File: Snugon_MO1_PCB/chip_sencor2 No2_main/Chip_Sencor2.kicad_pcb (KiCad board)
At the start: 2 copper layers, 50.7 x 80 mm, 55 parts, among them J1 Conn_01x8_Pin + 2, J3 USB_C_Receptacle_USB2.0, J6 Conn_01x8_Pin + 2, SW0 SW_PUSH, SW1 SW_PUSH, U1 RP2040, U2 TPS73601DBV, U3 TXS0102DCU, U4 TXS0102DCU, U5 PMW3360DM-T2QU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

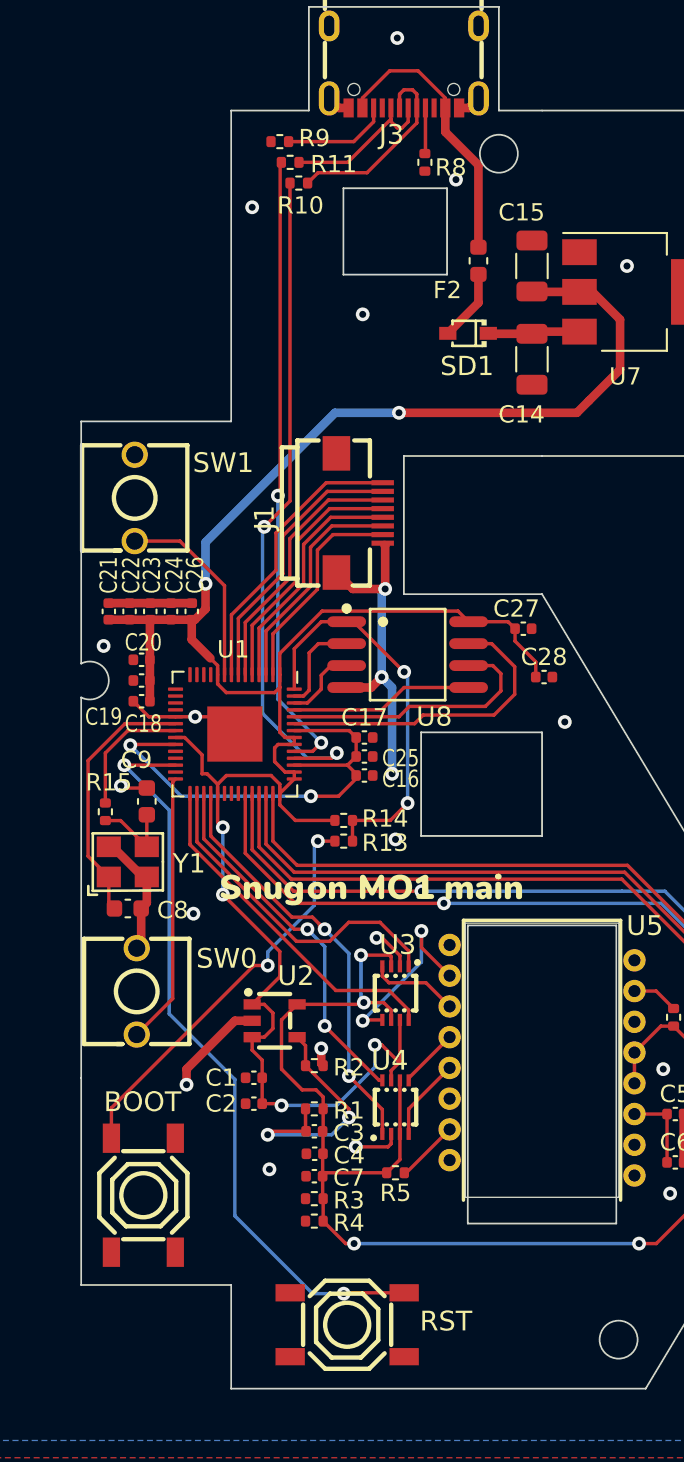
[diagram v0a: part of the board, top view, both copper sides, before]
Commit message: リセットボタンとブートボタンの配線修正
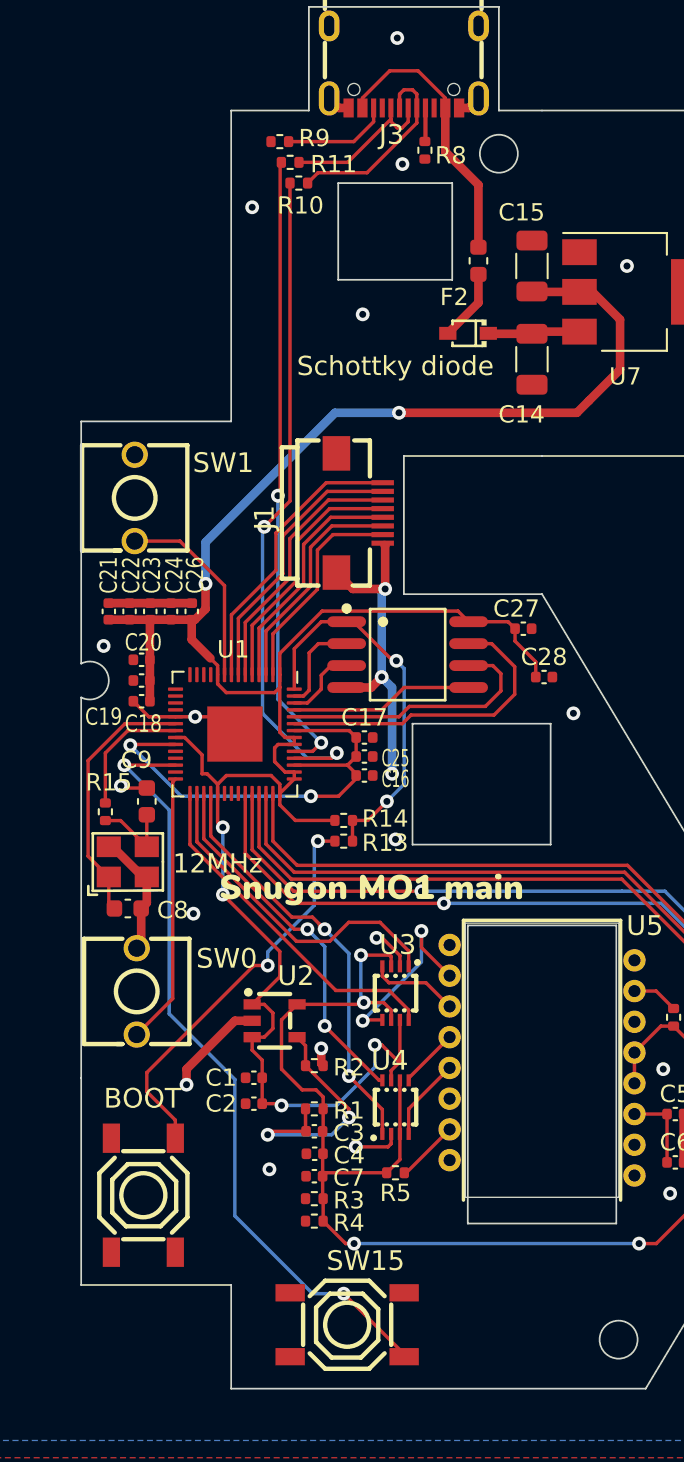
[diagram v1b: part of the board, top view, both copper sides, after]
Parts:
- removed RST: RESET, 0:SW-SMD_4P-L5.1-W5.1-P3.70-LS6.5-TL-2
- added SW15: RESET, 0:SW-SMD_4P-L5.1-W5.1-P3.70-LS6.5-TL-2, F.Cu at (125.4, 133.3)
- SD1: value SD1 -> Schottky diode
- U8: value U8 -> W25Q128JVSIQ
- Y1: value Y1 -> 12MHz
- moved R8 0.70 mm to (129.9, 65.3)
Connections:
- BOOT pad 2: USB_BOOT -> unconnected-(SW14-Pad2)
- BOOT pad 3: (no net) -> unconnected-(SW14-K-Pad3)
- BOOT pad 4: (no net) -> USB_BOOT
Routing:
- net RESET: track 43.4 -> 45.0 mm
- net QSPI_SS: track 23.0 -> 22.2 mm
- net Net-(J3-CC1): track 2.65 -> 1.95 mm
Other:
- outline, holes or cut-outs redrawn

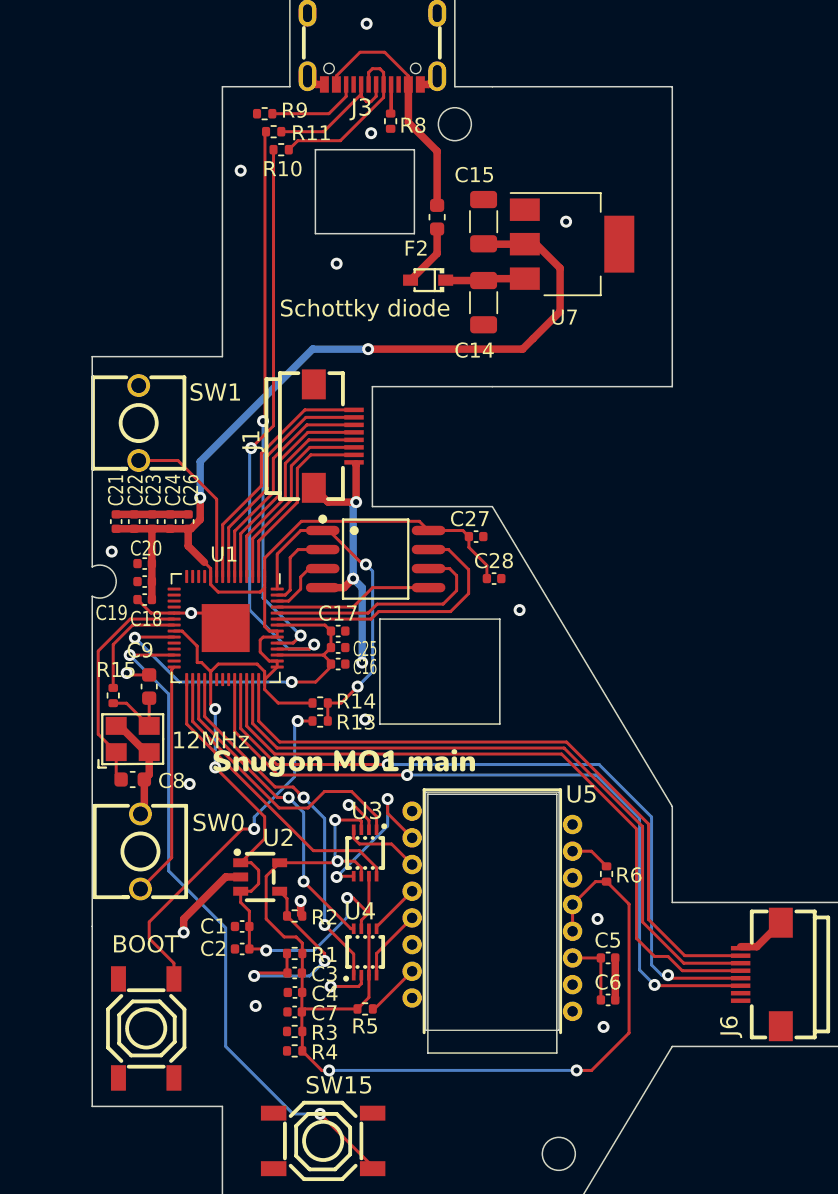
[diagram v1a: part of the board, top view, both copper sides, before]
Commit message: スイッチとエンコーダーはPCBAしない
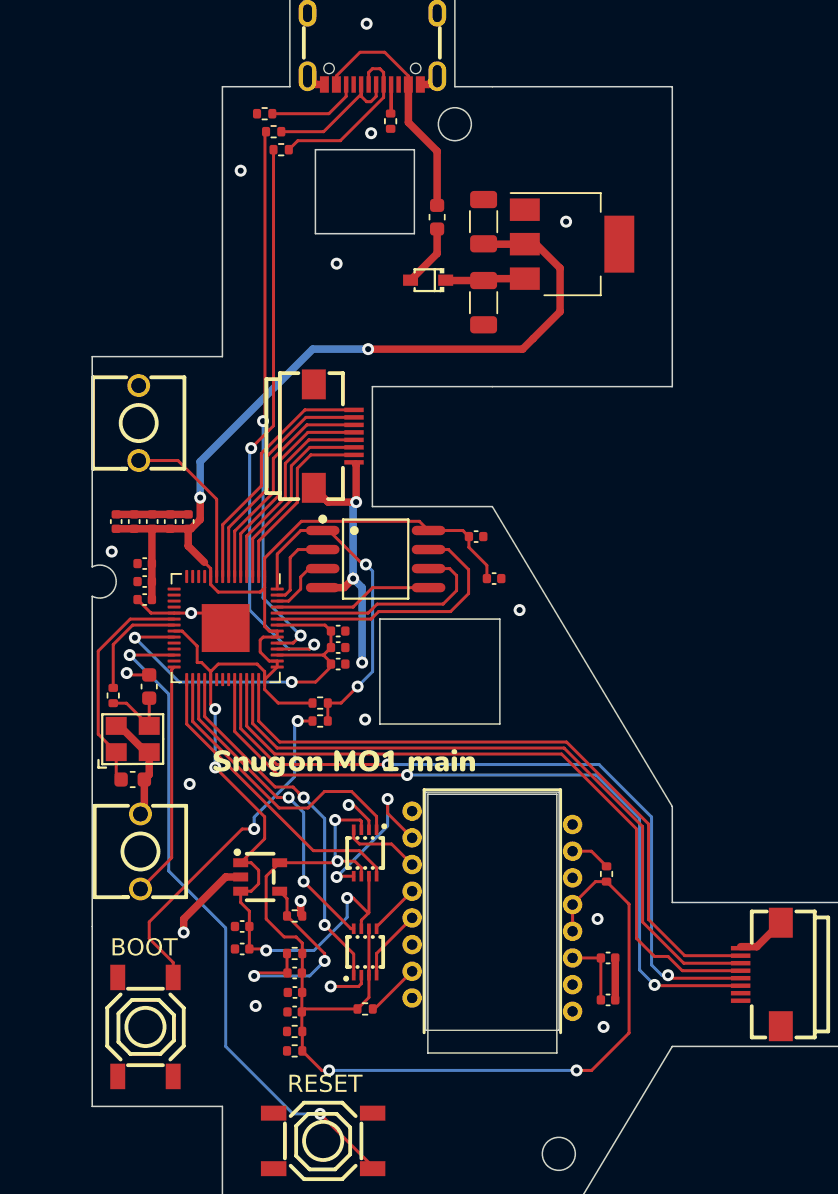
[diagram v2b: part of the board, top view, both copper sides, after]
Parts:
- removed BOOT: BOOT, 0:SW-SMD_4P-L5.1-W5.1-P3.70-LS6.5-TL-2
- added SW14: BOOT, 0:SW-SMD_4P-L5.1-W5.1-P3.70-LS6.5-TL-2, F.Cu at (113.5, 125.7)

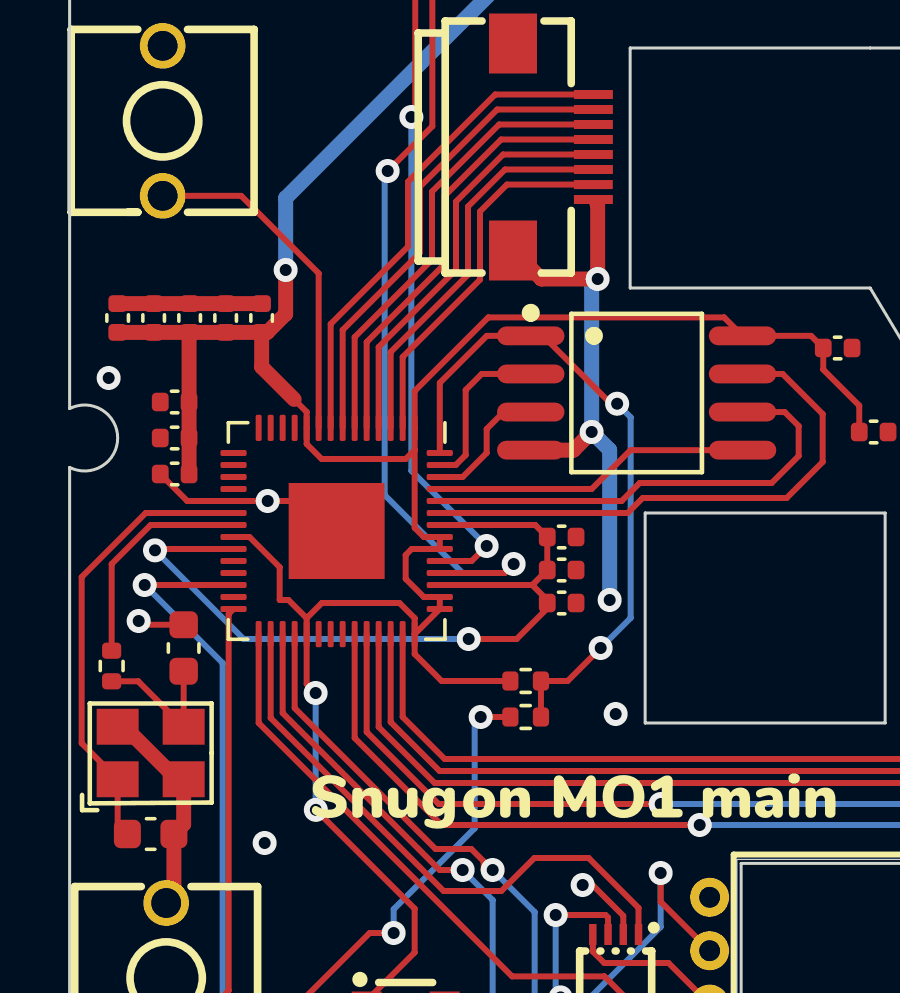
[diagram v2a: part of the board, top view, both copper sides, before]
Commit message: エンコーダの配線修正
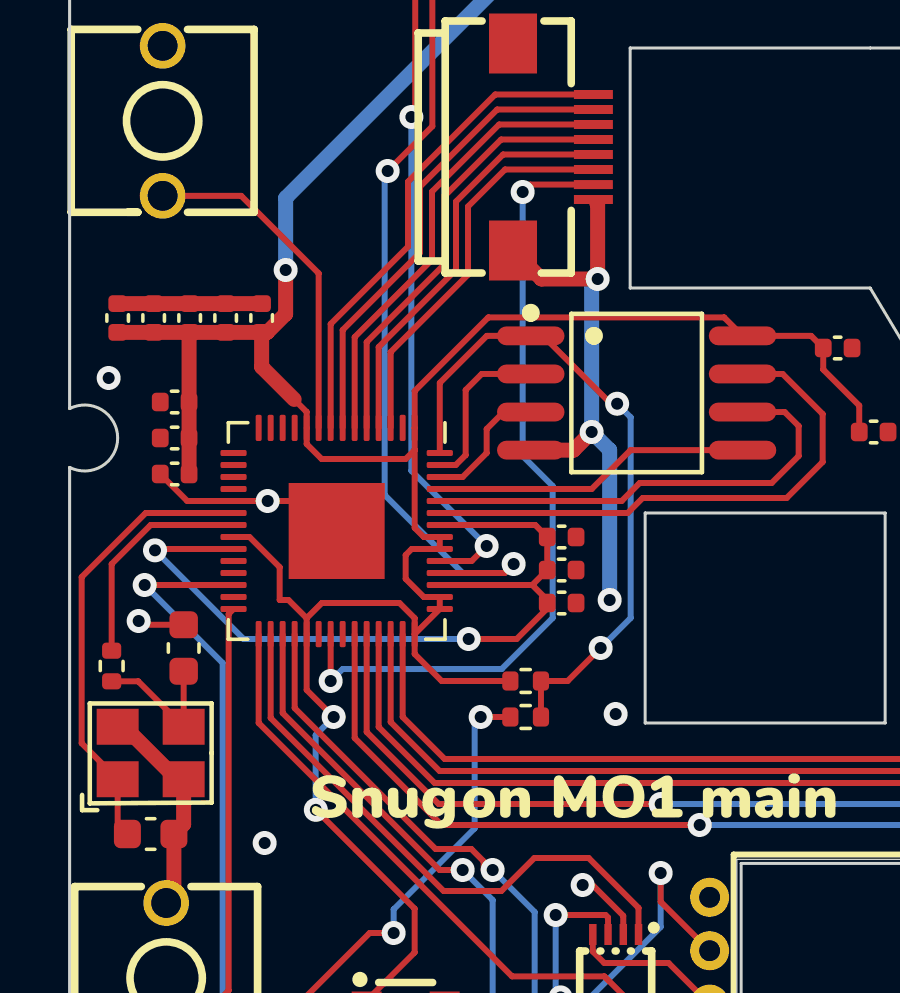
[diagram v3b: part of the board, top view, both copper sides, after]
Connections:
- U1 pad 2: RE0B -> unconnected-(U1-GPIO0-Pad2)
- U1 pad 35: unconnected-(U1-GPIO23-Pad35) -> RE0B
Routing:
- net RE0B: track 12.4 -> 26.9 mm, vias 0 -> 2
